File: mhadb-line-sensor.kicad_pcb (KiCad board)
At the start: 2 copper layers, 100 x 20 mm, 106 parts, among them J1 TC2030, J2 Conn_01x04_Pin, J3 Conn_01x04, J4 Conn_01x04_Pin, SW1 SW_Push, SW2 SW_Push, SW3 SW_Push, SW4 SW_Push, U1 HT753-1, U10 QRE1113GR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

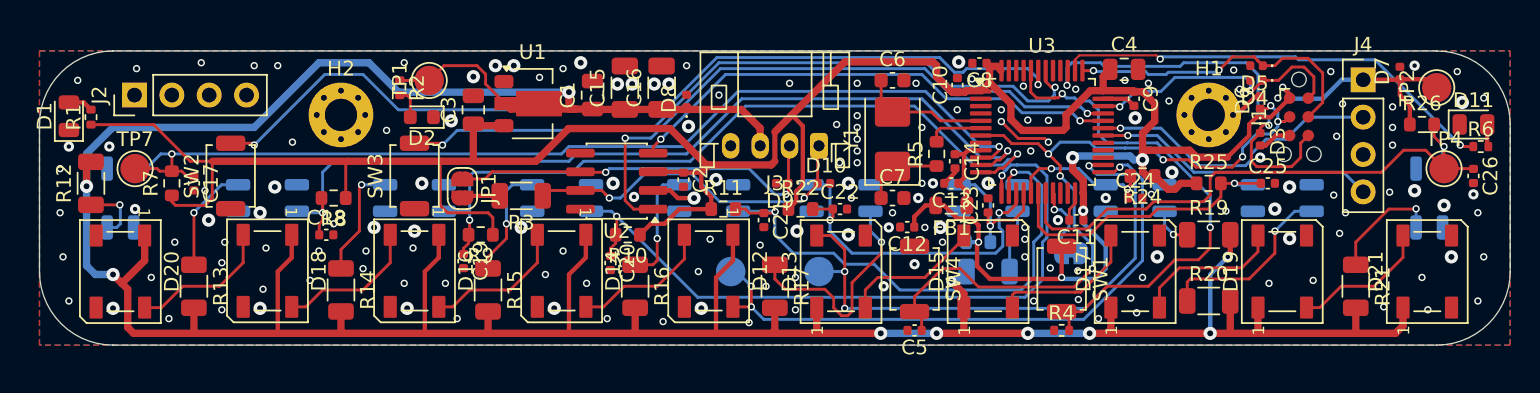
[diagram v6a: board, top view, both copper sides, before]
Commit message: pcb(silkscreen): clean reference designators
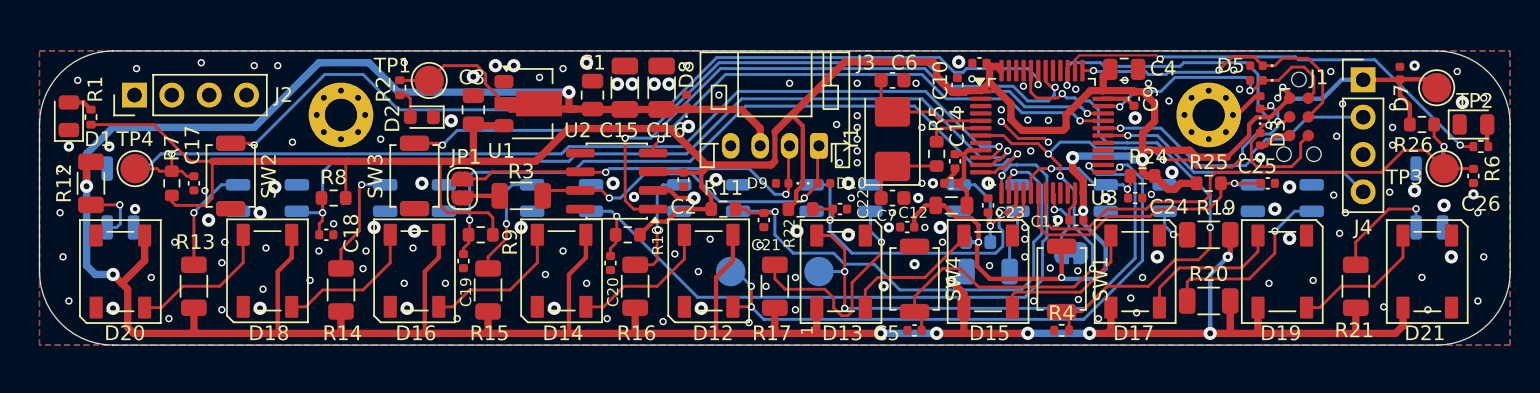
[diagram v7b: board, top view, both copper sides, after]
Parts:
- renumbered TP4 to TP3, TP7 to TP4, TP8 to TP5, TP9 to TP6
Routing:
- net GND: vias 167 -> 168
